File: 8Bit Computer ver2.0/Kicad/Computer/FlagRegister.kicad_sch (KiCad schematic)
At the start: 9 parts, among them IC125 SN74LVC1G14DBVR, IC126 SN74AHC32DR, IC127 SN74HCS4075DR, IC128 SN74AHC08DR, IC129 SN74AHC74DR, IC130 SN74AHC74DR, IC131 SN74AHC74DR, IC132 SN74AHC08DR, IC133 SN74ABT574ADWR

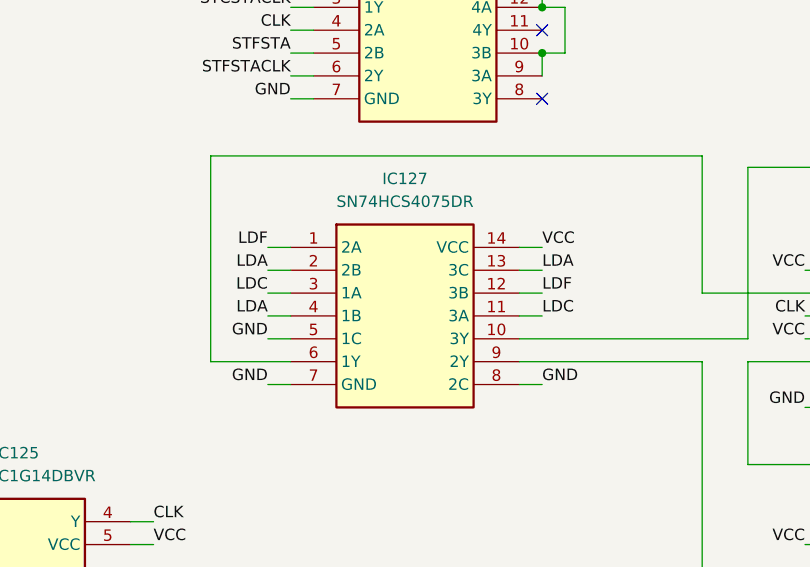
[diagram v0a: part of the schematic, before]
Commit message: Kicad
added 10pin 2,54mm Header
finished ALU PCB and added pin Header for extra use (DAT,ADR,CMD,Ddis,CLK)
31.12-06.01 about +60hr for ALU
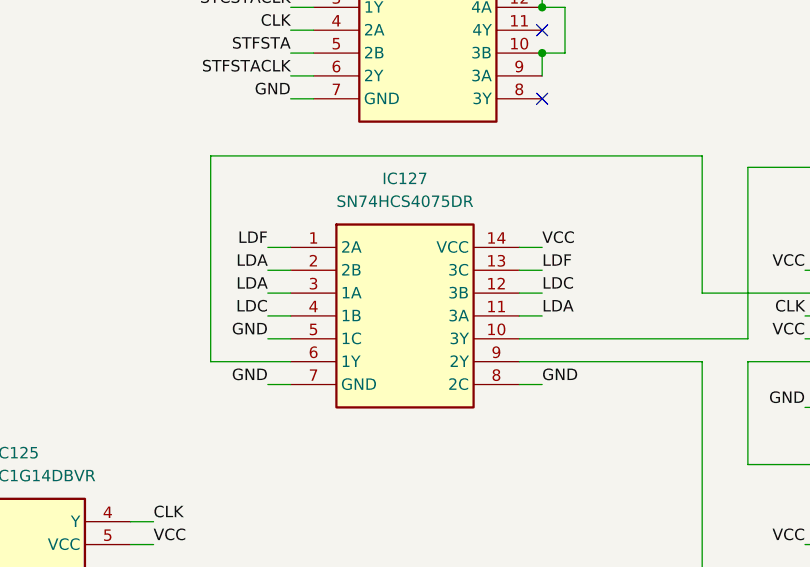
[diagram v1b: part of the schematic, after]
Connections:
- net LDA: now also IC127.11 (3A), IC127.3 (1A); no longer IC127.13 (3C), IC127.4 (1B)
- net LDC: now also IC127.12 (3B), IC127.4 (1B); no longer IC127.11 (3A), IC127.3 (1A)
- net LDF: now also IC127.13 (3C); no longer IC127.12 (3B)
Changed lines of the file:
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@@
+		)
+	)
+	(label "LDC"
+		(at 90.17 104.14 180)
+		(effects
+			(font
+				(size 1.27 1.27)
+			)
+			(justify right bottom)
 		)
 	)
@@
 		)
 	)
+	(label "LDC"
+		(at 120.65 101.6 0)
+		(effects
+			(font
+				(size 1.27 1.27)
+			)
+			(justify left bottom)
+		)
+	)
 	(label "VCC"
 		(at 77.47 129.54 0)
@@
 		)
 	)
+	(label "LDF"
+		(at 120.65 99.06 0)
+		(effects
+			(font
+				(size 1.27 1.27)
+			)
+			(justify left bottom)
+		)
+	)
 	(label "F"
 		(at 63.5 41.91 180)
@@
 		)
 	)
-	(label "LDA"
-		(at 90.17 104.14 180)
-		(effects
-			(font
-				(size 1.27 1.27)
-			)
-			(justify right bottom)
-		)
-	)
 	(label "DAT7"
 		(at 257.81 93.98 0)
@@
 		)
 	)
-	(label "LDF"
-		(at 120.65 101.6 0)
-		(effects
-			(font
-				(size 1.27 1.27)
-			)
-			(justify left bottom)
-		)
-	)
 	(label "LDA"
 		(at 90.17 99.06 180)
@@
 		)
 	)
-	(label "LDC"
-		(at 90.17 101.6 180)
-		(effects
-			(font
-				(size 1.27 1.27)
-			)
-			(justify right bottom)
-		)
-	)
 	(label "VCC"
 		(at 215.9 46.99 0)
@@
 		)
 	)
+	(label "LDA"
+		(at 120.65 104.14 0)
+		(effects
+			(font
+				(size 1.27 1.27)
+			)
+			(justify left bottom)
+		)
+	)
 	(label "CLK"
 		(at 149.86 104.14 180)
@@
 		)
 	)
-	(label "LDC"
-		(at 120.65 104.14 0)
-		(effects
-			(font
-				(size 1.27 1.27)
-			)
-			(justify left bottom)
-		)
-	)
 	(label "LDA"
-		(at 120.65 99.06 0)
-		(effects
-			(font
-				(size 1.27 1.27)
-			)
-			(justify left bottom)
-		)
-	)
+		(at 90.17 101.6 180)
+		(effects
+			(font
+				(size 1.27 1.27)
+			)
+			(justify right bottom)
+		)
+	)

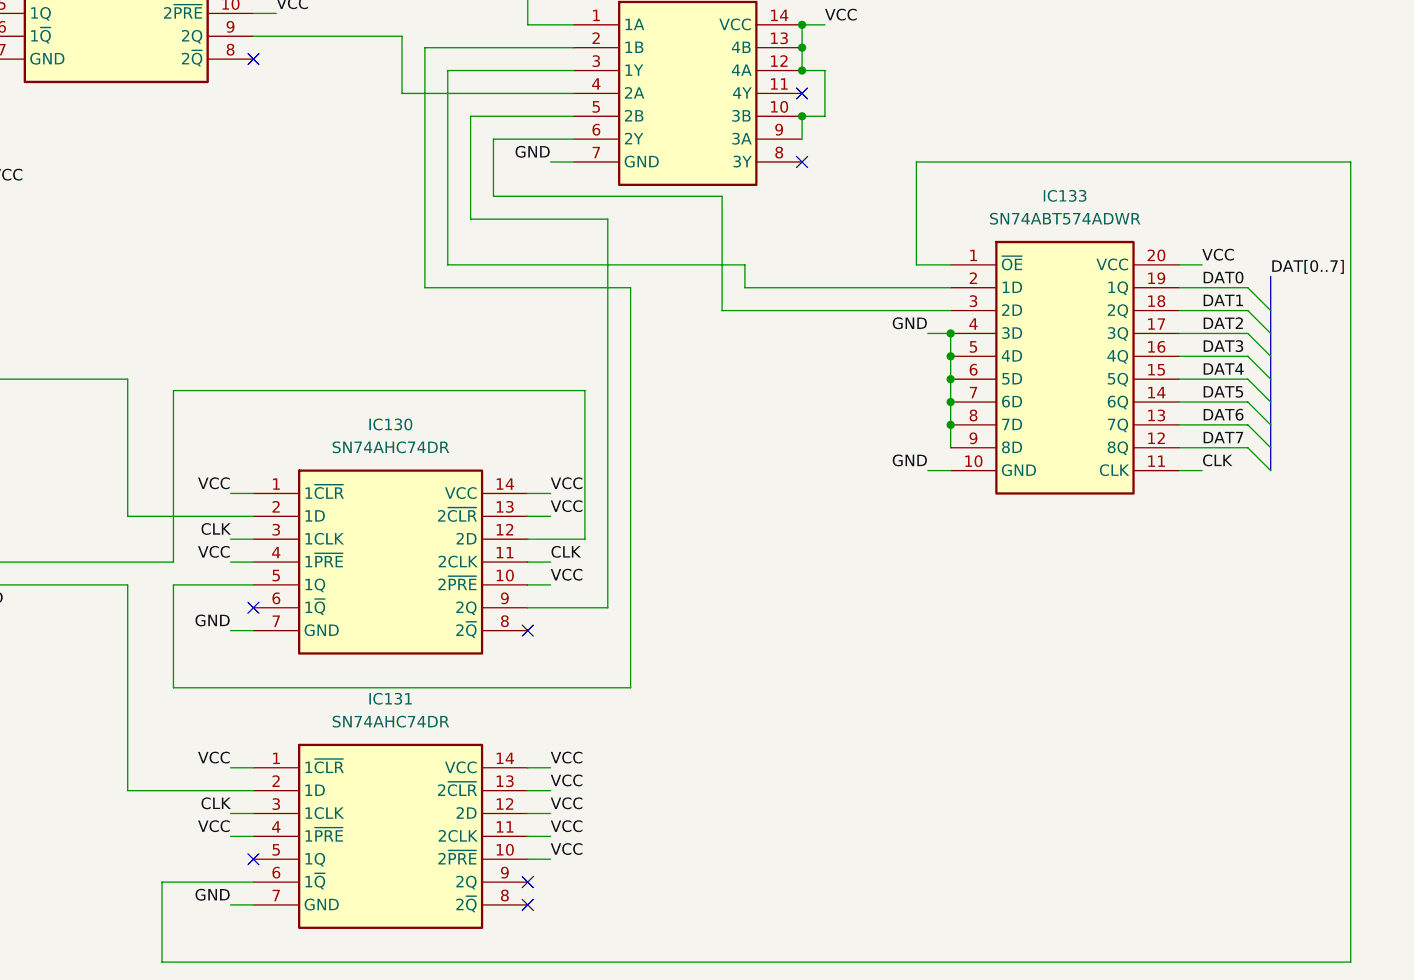
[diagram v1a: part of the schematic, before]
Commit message: Kicad Fixes only schematic
fixed important schematic errors
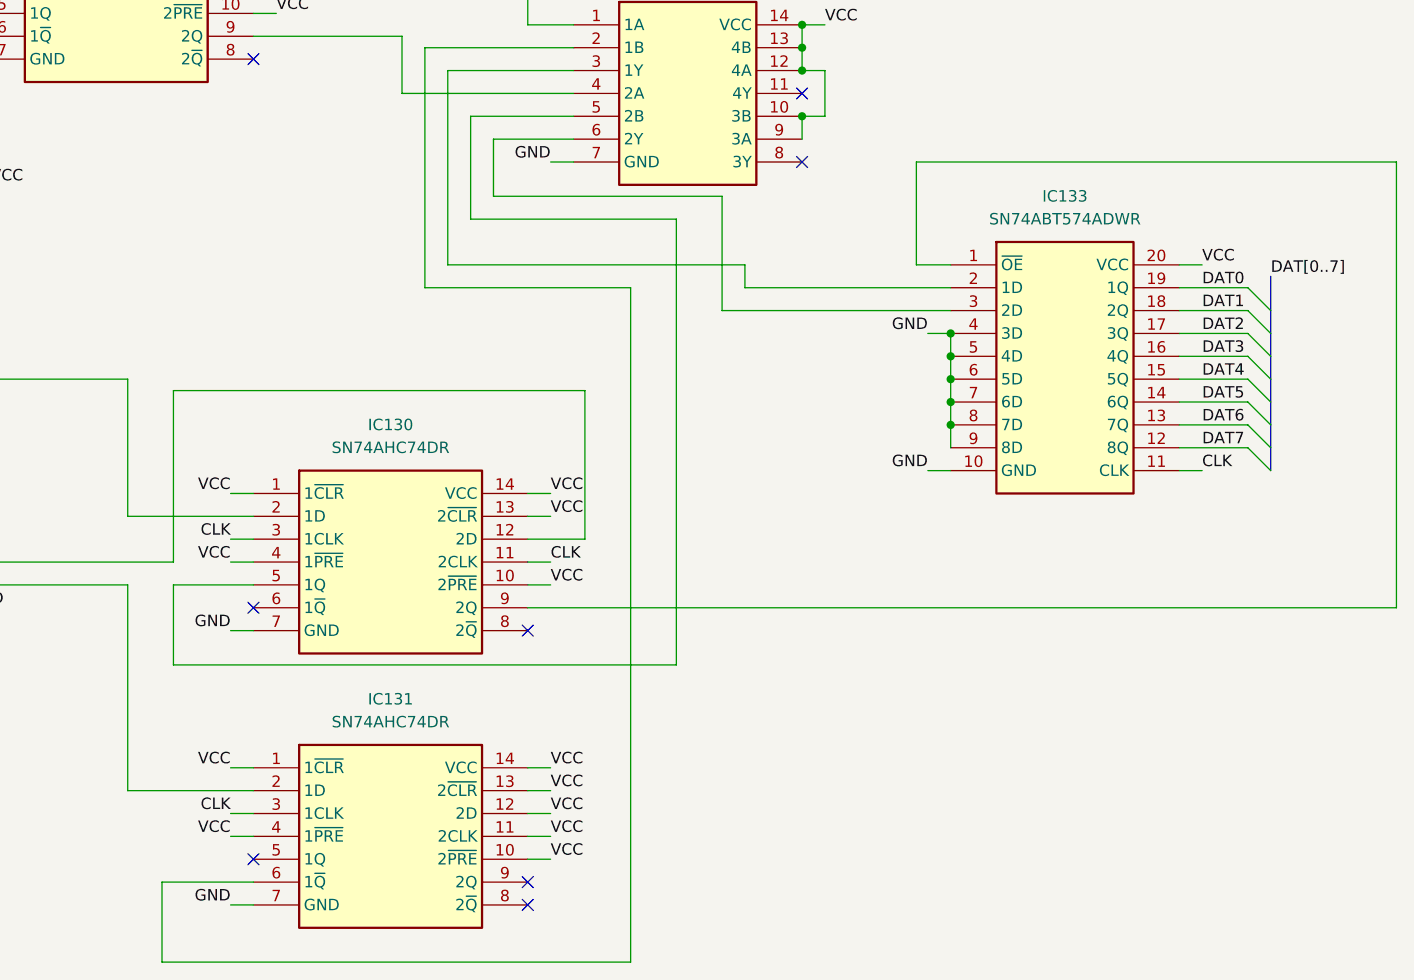
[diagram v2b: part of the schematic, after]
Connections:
- net at IC133.1 (~{OE}): now also IC130.9 (2Q); no longer IC131.6 (1~{Q})
- net at IC130.5 (1Q): now also IC132.5 (2B); no longer IC132.2 (1B)
- new net: IC131.6 (1~{Q}), IC132.2 (1B)
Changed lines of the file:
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@@
+	(wire
+		(pts
+			(xy 182.88 111.76) (xy 279.4 111.76)
+		)
+		(stroke
+			(width 0)
+			(type default)
+		)
+	)
 	(wire
 		(pts
@@
 	(wire
 		(pts
-			(xy 143.51 120.65) (xy 194.31 120.65)
-		)
-		(stroke
-			(width 0)
-			(type default)
-		)
-	)
-	(wire
-		(pts
 			(xy 90.17 101.6) (xy 92.71 101.6)
 		)
@@
 	(wire
 		(pts
-			(xy 274.32 62.23) (xy 226.06 62.23)
+			(xy 226.06 62.23) (xy 226.06 73.66)
 		)
 		(stroke
@@
 	(wire
 		(pts
+			(xy 199.39 118.11) (xy 199.39 68.58)
+		)
+		(stroke
+			(width 0)
+			(type default)
+		)
+	)
+	(wire
+		(pts
 			(xy 152.4 106.68) (xy 149.86 106.68)
 		)
@@
 	(wire
 		(pts
+			(xy 143.51 118.11) (xy 199.39 118.11)
+		)
+		(stroke
+			(width 0)
+			(type default)
+		)
+	)
+	(wire
+		(pts
 			(xy 182.88 109.22) (xy 185.42 109.22)
 		)
@@
 	(wire
 		(pts
+			(xy 279.4 111.76) (xy 279.4 62.23)
+		)
+		(stroke
+			(width 0)
+			(type default)
+		)
+	)
+	(wire
+		(pts
 			(xy 138.43 86.36) (xy 138.43 101.6)
 		)
@@
 	(wire
 		(pts
-			(xy 194.31 120.65) (xy 194.31 76.2)
-		)
-		(stroke
-			(width 0)
-			(type default)
-		)
-	)
-	(wire
-		(pts
 			(xy 204.47 66.04) (xy 179.07 66.04)
 		)
@@
 	(wire
 		(pts
-			(xy 142.24 151.13) (xy 274.32 151.13)
+			(xy 142.24 151.13) (xy 194.31 151.13)
+		)
+		(stroke
+			(width 0)
+			(type default)
+		)
+	)
+	(wire
+		(pts
+			(xy 279.4 62.23) (xy 226.06 62.23)
 		)
 		(stroke
@@
 	(wire
 		(pts
-			(xy 182.88 111.76) (xy 191.77 111.76)
-		)
-		(stroke
-			(width 0)
-			(type default)
-		)
-	)
-	(wire
-		(pts
 			(xy 31.75 102.87) (xy 36.83 102.87)
 		)
@@
 	(wire
 		(pts
-			(xy 143.51 109.22) (xy 143.51 120.65)
-		)
-		(stroke
-			(width 0)
-			(type default)
-		)
-	)
-	(wire
-		(pts
 			(xy 58.42 39.37) (xy 66.04 39.37)
 		)
@@
 		)
 	)
+	(wire
+		(pts
+			(xy 143.51 109.22) (xy 143.51 118.11)
+		)
+		(stroke
+			(width 0)
+			(type default)
+		)
+	)
 	(bus
 		(pts
@@
 	(wire
 		(pts
-			(xy 191.77 111.76) (xy 191.77 68.58)
-		)
-		(stroke
-			(width 0)
-			(type default)
-		)
-	)
-	(wire
-		(pts
 			(xy 182.88 134.62) (xy 185.42 134.62)
 		)
@@
 	(wire
 		(pts
-			(xy 274.32 151.13) (xy 274.32 62.23)
-		)
-		(stroke
-			(width 0)
-			(type default)
-		)
-	)
-	(wire
-		(pts
 			(xy 31.75 50.8) (xy 36.83 50.8)
 		)
@@
 	(wire
 		(pts
-			(xy 226.06 62.23) (xy 226.06 73.66)
-		)
-		(stroke
-			(width 0)
-			(type default)
-		)
-	)
-	(wire
-		(pts
 			(xy 91.44 41.91) (xy 93.98 41.91)
 		)
@@
 	(wire
 		(pts
-			(xy 191.77 68.58) (xy 176.53 68.58)
+			(xy 176.53 68.58) (xy 199.39 68.58)
 		)
 		(stroke
@@
 		)
 		(stroke
+			(width 0)
+			(type default)
+		)
+	)
+	(wire
+		(pts
+			(xy 194.31 76.2) (xy 194.31 151.13)
+		)
+		(stroke

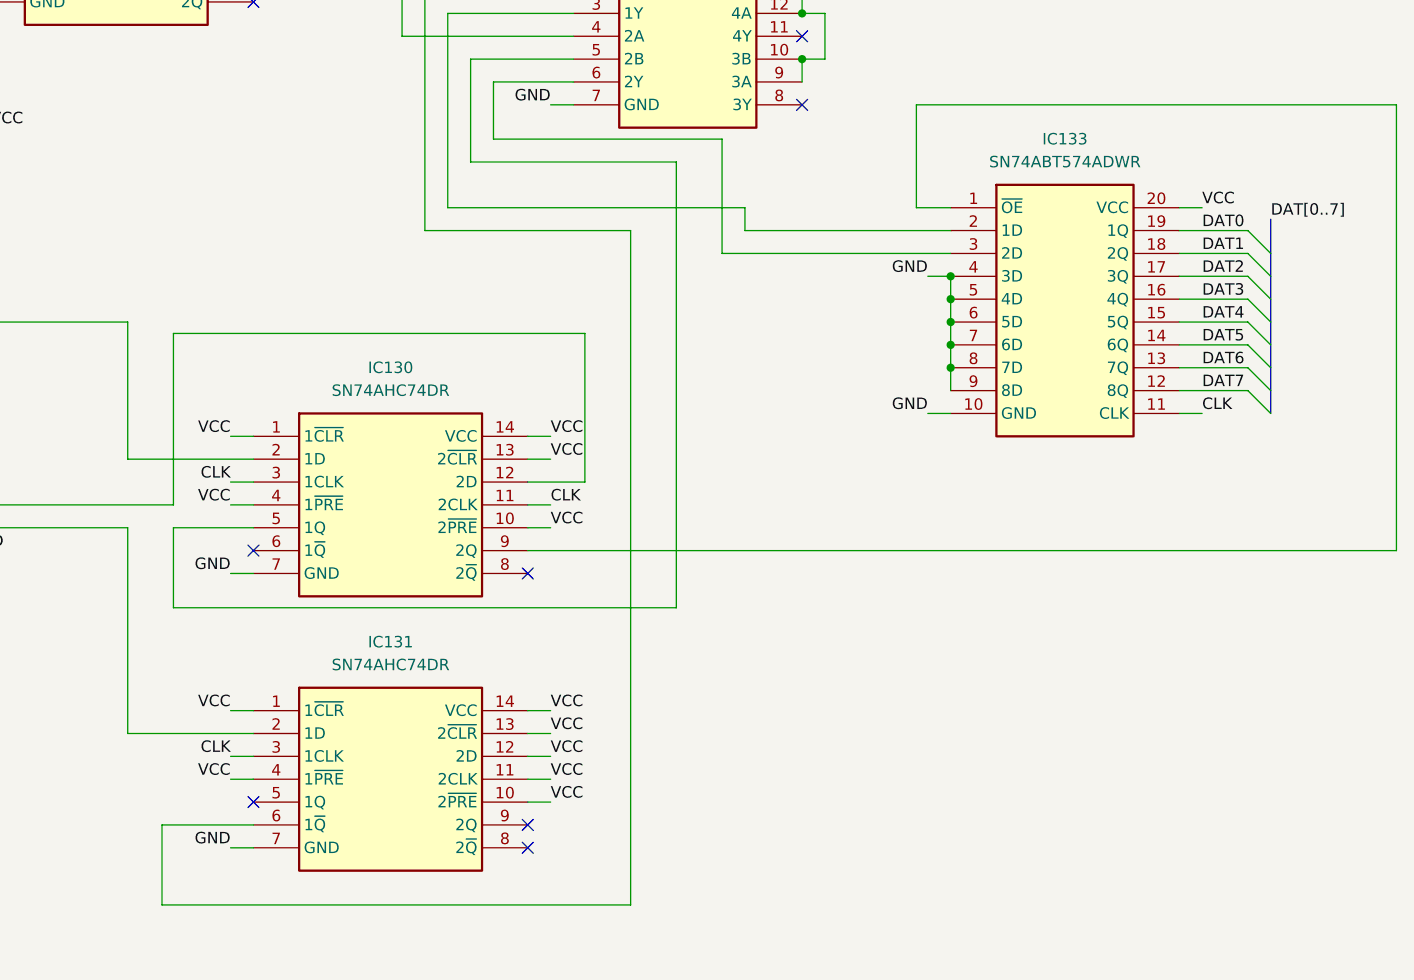
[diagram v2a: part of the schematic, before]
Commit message: Kicad, PCB Fix
fixed the errors on the PCB
added mounting holes
added GND panels on Top and Bot Layer
added 100uF
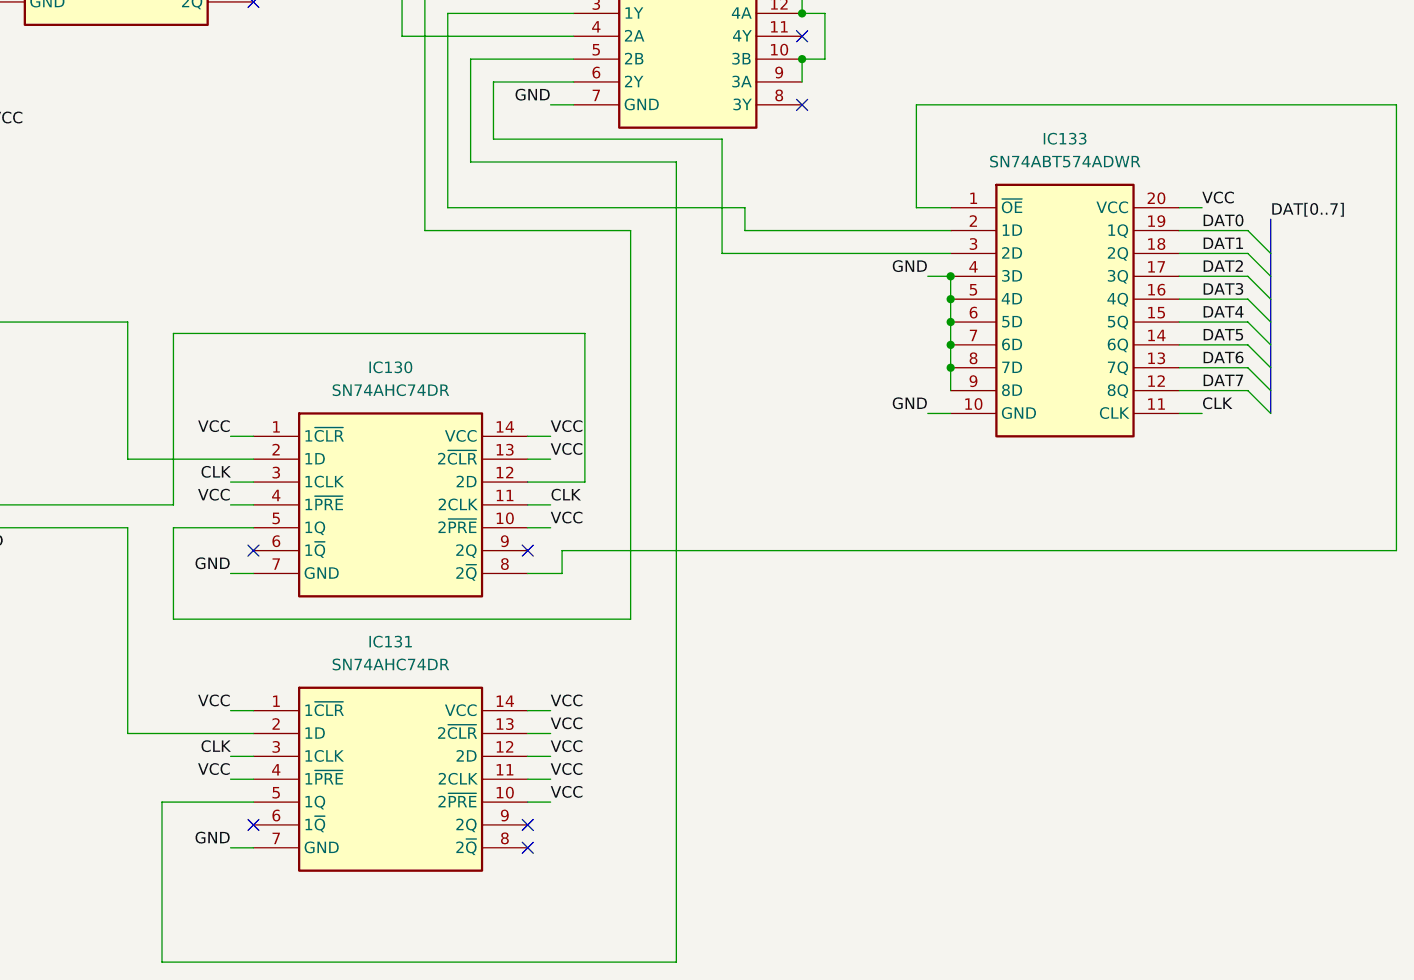
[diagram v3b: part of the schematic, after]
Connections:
- net at IC133.1 (~{OE}): now also IC130.8 (2~{Q}); no longer IC130.9 (2Q)
- net at IC130.5 (1Q): now also IC132.2 (1B); no longer IC132.5 (2B)
- net at IC131.5 (1Q): now also IC132.5 (2B)
- net at IC131.6 (1~{Q}): no longer IC132.2 (1B)
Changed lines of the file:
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@@
+	)
+	(no_connect
+		(at 182.88 111.76)
 	)
 	(no_connect
@@
 	)
 	(no_connect
-		(at 182.88 114.3)
-	)
-	(no_connect
-		(at 152.4 139.7)
-	)
-	(no_connect
 		(at 152.4 50.8)
 	)
@@
 	(no_connect
 		(at 120.65 80.01)
+	)
+	(no_connect
+		(at 152.4 142.24)
 	)
 	(no_connect
@@
 	(wire
 		(pts
-			(xy 182.88 111.76) (xy 279.4 111.76)
-		)
-		(stroke
-			(width 0)
-			(type default)
-		)
-	)
-	(wire
-		(pts
-			(xy 152.4 142.24) (xy 142.24 142.24)
-		)
-		(stroke
-			(width 0)
-			(type default)
-		)
-	)
-	(wire
-		(pts
 			(xy 187.96 52.07) (xy 173.99 52.07)
 		)
@@
 	(wire
 		(pts
+			(xy 143.51 119.38) (xy 143.51 109.22)
+		)
+		(stroke
+			(width 0)
+			(type default)
+		)
+	)
+	(wire
+		(pts
 			(xy 226.06 62.23) (xy 226.06 73.66)
 		)
@@
 	(wire
 		(pts
+			(xy 142.24 157.48) (xy 142.24 139.7)
+		)
+		(stroke
+			(width 0)
+			(type default)
+		)
+	)
+	(wire
+		(pts
 			(xy 255.27 81.28) (xy 262.89 81.28)
 		)
@@
 	(wire
 		(pts
-			(xy 199.39 118.11) (xy 199.39 68.58)
+			(xy 199.39 68.58) (xy 199.39 157.48)
 		)
 		(stroke
@@
 	(wire
 		(pts
-			(xy 143.51 118.11) (xy 199.39 118.11)
-		)
-		(stroke
-			(width 0)
-			(type default)
-		)
-	)
-	(wire
-		(pts
 			(xy 182.88 109.22) (xy 185.42 109.22)
 		)
@@
 	(wire
 		(pts
-			(xy 142.24 151.13) (xy 194.31 151.13)
-		)
-		(stroke
-			(width 0)
-			(type default)
-		)
-	)
-	(wire
-		(pts
 			(xy 279.4 62.23) (xy 226.06 62.23)
 		)
@@
 	(wire
 		(pts
-			(xy 142.24 142.24) (xy 142.24 151.13)
-		)
-		(stroke
-			(width 0)
-			(type default)
-		)
-	)
-	(wire
-		(pts
 			(xy 255.27 76.2) (xy 262.89 76.2)
 		)
@@
 	(wire
 		(pts
+			(xy 194.31 119.38) (xy 143.51 119.38)
+		)
+		(stroke
+			(width 0)
+			(type default)
+		)
+	)
+	(wire
+		(pts
 			(xy 123.19 74.93) (xy 123.19 69.85)
 		)
@@
 	(wire
 		(pts
-			(xy 143.51 109.22) (xy 143.51 118.11)
+			(xy 182.88 114.3) (xy 186.69 114.3)
 		)
 		(stroke
@@
 	(wire
 		(pts
+			(xy 199.39 157.48) (xy 142.24 157.48)
+		)
+		(stroke
+			(width 0)
+			(type default)
+		)
+	)
+	(wire
+		(pts
 			(xy 182.88 132.08) (xy 185.42 132.08)
 		)
@@
 	(wire
 		(pts
+			(xy 186.69 111.76) (xy 186.69 114.3)
+		)
+		(stroke
+			(width 0)
+			(type default)
+		)
+	)
+	(wire
+		(pts
 			(xy 182.88 25.4) (xy 182.88 46.99)
 		)
@@
 	(wire
 		(pts
+			(xy 152.4 139.7) (xy 142.24 139.7)
+		)
+		(stroke
+			(width 0)
+			(type default)
+		)
+	)
+	(wire
+		(pts
 			(xy 182.88 137.16) (xy 185.42 137.16)
 		)
@@
 	(wire
 		(pts
+			(xy 186.69 111.76) (xy 279.4 111.76)
+		)
+		(stroke
+			(width 0)
+			(type default)
+		)
+	)
+	(wire
+		(pts
 			(xy 63.5 36.83) (xy 66.04 36.83)
 		)
@@
 	(wire
 		(pts
-			(xy 194.31 76.2) (xy 194.31 151.13)
-		)
-		(stroke
+			(xy 194.31 76.2) (xy 194.31 119.38)
+		)
+		(stroke
